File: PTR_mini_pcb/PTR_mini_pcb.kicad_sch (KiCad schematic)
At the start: 42 parts, among them J1 ESP32_PROG_CON, J3 67996-104HLF, U1 ESP32-S3FN8, Y2 X1G0054210307

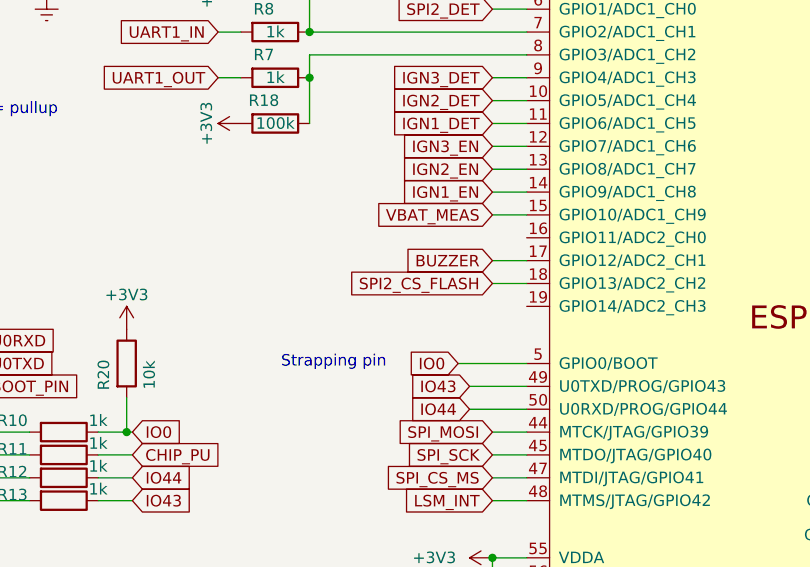
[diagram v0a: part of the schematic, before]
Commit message: SPI Flash moved to different SPI lines
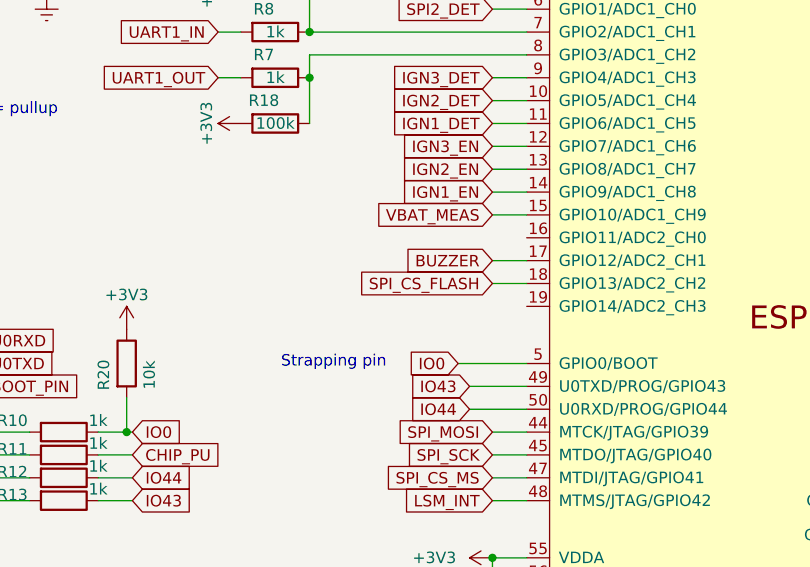
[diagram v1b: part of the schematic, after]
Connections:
- net SPI2_CS_FLASH renamed SPI_CS_FLASH
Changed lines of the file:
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@@
 		)
 	)
-	(global_label "SPI2_CS_FLASH"
+	(global_label "SPI_CS_FLASH"
 		(shape input)
 		(at 105.41 87.63 180)
@@
 		)
 		(property "Intersheetrefs" "${INTERSHEET_REFS}"
-			(at 87.971 87.63 0)
+			(at 89.1805 87.63 0)
 			(hide yes)
 			(show_name no)

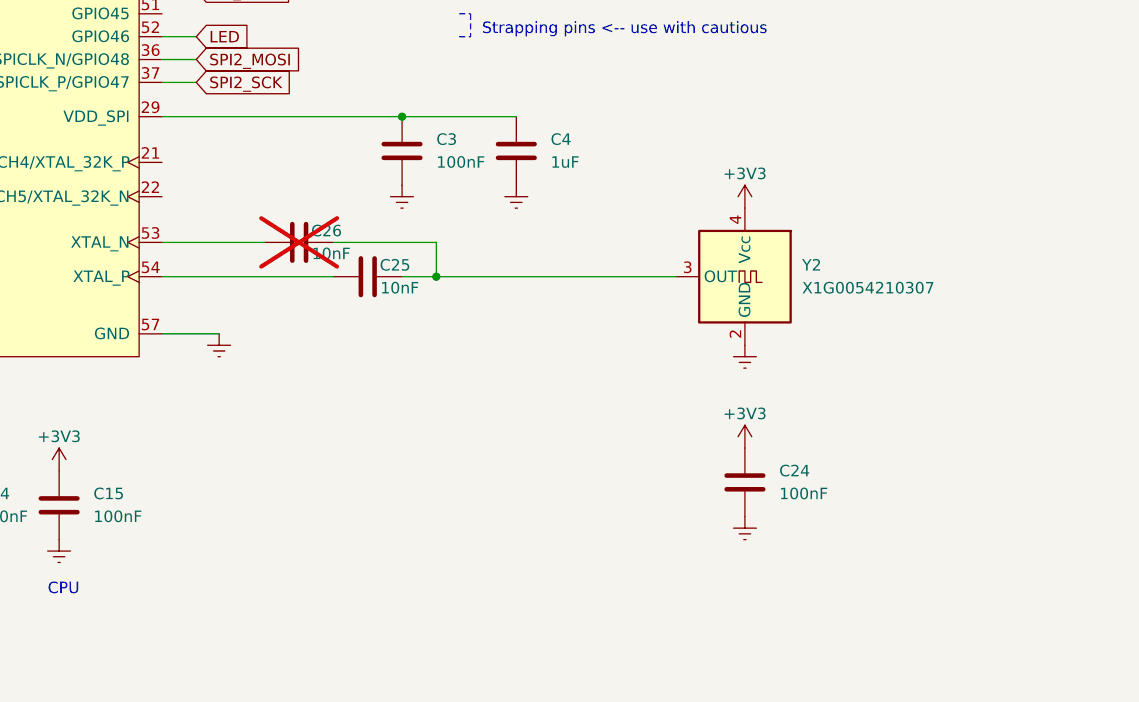
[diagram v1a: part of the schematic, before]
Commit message: TCXO replaced with 10ppm crystal
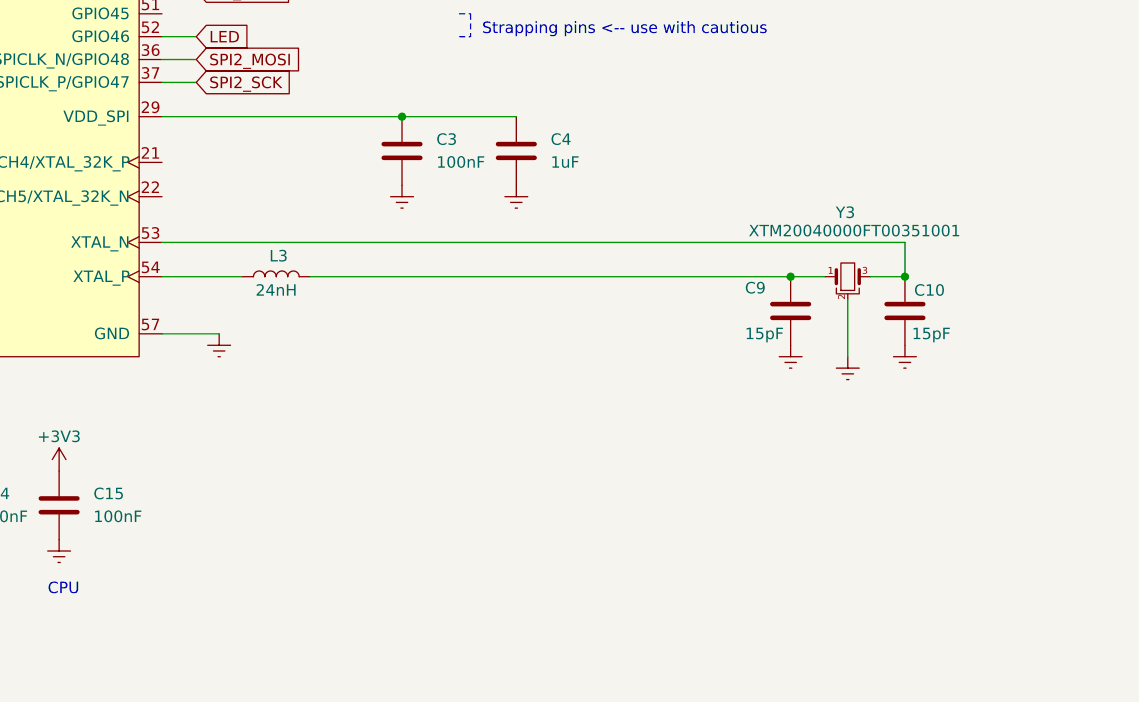
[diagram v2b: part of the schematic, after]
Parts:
- removed C24: 100nF, Capacitor_SMD:C_0402_1005Metric, symbol Device:C
- removed C25, C26: 10nF, Capacitor_SMD:C_0402_1005Metric, symbol Device:C
- removed Y2: X1G0054210307, Oscillator:Oscillator_SMD_SeikoEpson_TG2520SMN-xxx-xxxxxx-4Pin_2.5x2.0mm, symbol Oscillator:TG2520SMN-xx.xxxxxxMhz-xxxxNM
- added C10, C9: 15pF, Capacitor_SMD:C_0402_1005Metric, symbol Device:C
- added L3: 24nH, Inductor_SMD:L_0402_1005Metric, symbol Device:L
- added Y3: XTM20040000FT00351001, Crystal:Crystal_SMD_2016-4Pin_2.0x1.6mm, symbol KP-PTR_lib:XRCGB40M000F4M00R0
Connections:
- net Earth: now also C10.2, C9.1, Y3.2, Y3.4
- net at U1.53 (XTAL_N): now also C10.1, Y3.3
- net at U1.54 (XTAL_P): now also L3.1
- new net: C9.2, L3.2, Y3.1
